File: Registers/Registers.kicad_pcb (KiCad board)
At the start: 2 copper layers, 89.5 x 49.2 mm, 31 parts, among them J1 Conn_01x08_Socket, J2 Conn_01x08_Socket, J3 Conn_01x06_Pin, U1 SN74HCT245N, U2 74LS173, U3 74LS173

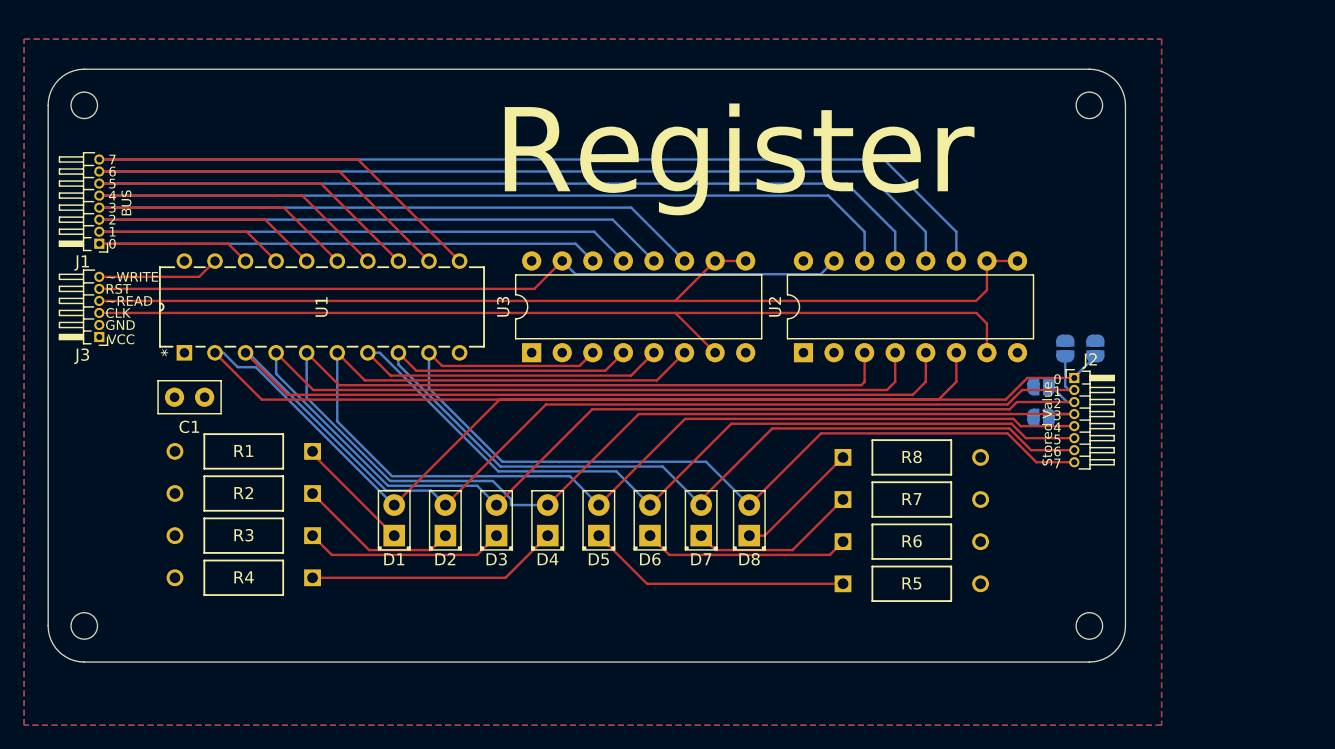
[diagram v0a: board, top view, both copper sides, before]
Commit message: Finished routing for registers. Silkscreen and PCB shape needs to be finalized.
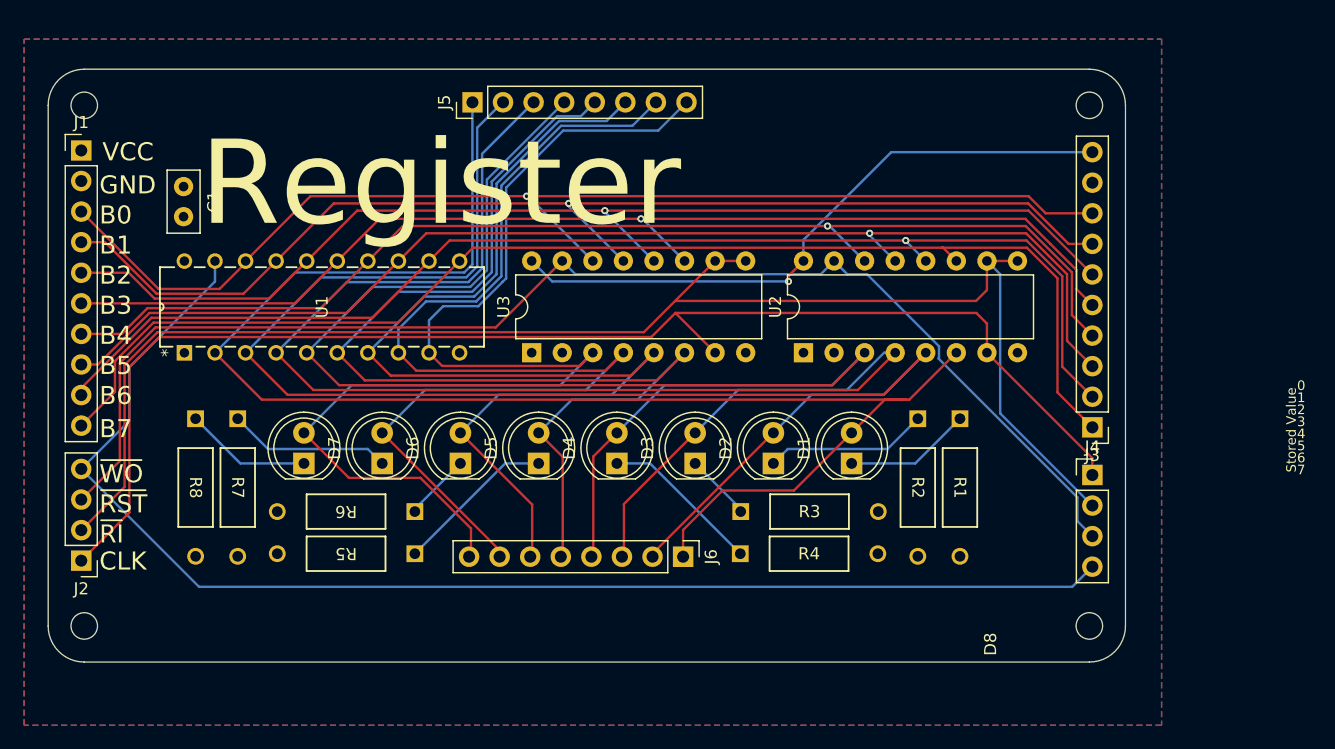
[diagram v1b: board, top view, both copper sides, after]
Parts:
- removed JP1, JP2, JP3, JP4: SolderJumper_2_Open, Jumper:SolderJumper-2_P1.3mm_Open_RoundedPad1.0x1.5mm
- added J4: Conn_01x04_Pin, Connector_PinHeader_2.54mm:PinHeader_1x04_P2.54mm_Vertical, F.Cu at (149.0, 74.0)
- added J5: Conn_01x08_Pin, Connector_PinHeader_2.54mm:PinHeader_1x08_P2.54mm_Vertical, F.Cu at (97.5, 43.0)
- added J6: Conn_01x08_Pin, Connector_PinHeader_2.54mm:PinHeader_1x08_P2.54mm_Vertical, F.Cu at (115.0, 80.8)
- D1, D2, D3, D4, D5, D6, D7, D8: footprint LED_THT:LED_D2.0mm_W4.8mm_H2.5mm_FlatTop -> LED_THT:LED_D5.0mm
- J1: value Conn_01x08_Socket -> Conn_01x10_Pin; footprint Connector_PinHeader_1.00mm:PinHeader_1x08_P1.00mm_Horizontal -> Connector_PinHeader_2.54mm:PinHeader_1x10_P2.54mm_Vertical
- J2: value Conn_01x08_Socket -> Conn_01x04_Pin; footprint Connector_PinHeader_1.00mm:PinHeader_1x08_P1.00mm_Horizontal -> Connector_PinHeader_2.54mm:PinHeader_1x04_P2.54mm_Vertical
- J3: value Conn_01x06_Pin -> Conn_01x10_Pin; footprint Connector_PinHeader_1.00mm:PinHeader_1x06_P1.00mm_Horizontal -> Connector_PinHeader_2.54mm:PinHeader_1x10_P2.54mm_Vertical
- moved J2 83.9 mm to (65.0, 81.1), turned to 180 degrees
- moved J3 82.8 mm to (149.0, 70.0)
- moved R8 53.9 mm to (74.5, 69.3), turned to -90 degrees
- moved R1 53.9 mm to (138.0, 69.3), turned to -90 degrees
- moved R7 50.7 mm to (78.0, 69.3), turned to -90 degrees
- moved R2 50.7 mm to (134.5, 69.3), turned to -90 degrees
- moved D1 38.5 mm to (129.0, 73.0)
- moved D8 37.5 mm to (83.5, 73.0)
- moved R5 35.7 mm to (92.7, 80.5), turned to 180 degrees
- moved R6 35.7 mm to (92.7, 77.0), turned to 180 degrees
- moved R3 35.6 mm to (119.8, 77.0), turned to 0 degrees
- moved R4 35.6 mm to (119.8, 80.5), turned to 0 degrees
- moved D2 27.9 mm to (122.5, 73.0)
- moved D7 27.2 mm to (90.0, 73.0)
- moved C1 17.6 mm to (73.5, 50.0), turned to -90 degrees
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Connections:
- J1 pad 1: /Bus0 -> +5V
- J1 pad 2: /Bus1 -> GND
- J1 pad 3: /Bus2 -> /Bus0
- J1 pad 4: /Bus3 -> /Bus1
- J1 pad 5: /Bus4 -> /Bus2
- J1 pad 6: /Bus5 -> /Bus3
- J1 pad 7: /Bus6 -> /Bus4
- J1 pad 8: /Bus7 -> /Bus5
- J2 pad 1: Net-(D1-A) -> /CLK
- J2 pad 2: Net-(D2-A) -> /~{READ}
- J2 pad 3: Net-(D3-A) -> /RST
- J2 pad 4: Net-(D4-A) -> /~{WRITE}
- J3 pad 1: +5V -> /Bus7
- J3 pad 2: GND -> /Bus6
- J3 pad 3: /CLK -> /Bus5
- J3 pad 4: /~{READ} -> /Bus4
- J3 pad 5: /RST -> /Bus3
- J3 pad 6: /~{WRITE} -> /Bus2
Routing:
- net /~{WRITE}: track 10.2 -> 110.6 mm
- net +5V: track 0.00 -> 53.0 mm, vias 0 -> 1
- net /RST: track 62.9 -> 109.2 mm
- net /Bus0: track 54.3 -> 98.6 mm, vias 0 -> 1
- net /~{READ}: track 86.3 -> 125.6 mm
- net /Bus1: track 60.2 -> 96.9 mm, vias 0 -> 1
- net /CLK: track 81.2 -> 112.1 mm
- net /Bus2: track 66.2 -> 96.0 mm, vias 0 -> 1
- net /Bus3: track 72.1 -> 96.3 mm, vias 0 -> 1
- net Net-(D1-A): track 149.8 -> 127.9 mm
- net Net-(D8-A): track 78.6 -> 96.9 mm
- net Net-(D2-A): track 142.2 -> 126.0 mm
- net Net-(D5-A): track 103.8 -> 91.2 mm
- net Net-(D3-A): track 134.2 -> 121.8 mm
- net Net-(D6-K): track 17.2 -> 5.57 mm
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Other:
- board text added: "B0"
- board text added: "B1"
- board text added: "B2"
- board text added: "B3"
- board text added: "B4"
- board text added: "B5"
- board text added: "B6"
- board text added: "B7"
- board text added: "~{RI}"
- board text added: "~{RST}"
- board text added: "~{WO}"
- board text removed: "BUS"
- board text removed: "NOTE: I don't think I ordered the D-registers. I think I got ALUs by acciedent instead."
- board text removed: "RST"
- board text removed: "TODO: Update for instruction register"
- board text removed: "~READ"
- board text removed: "~WRITE"

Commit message: Register layout complete.
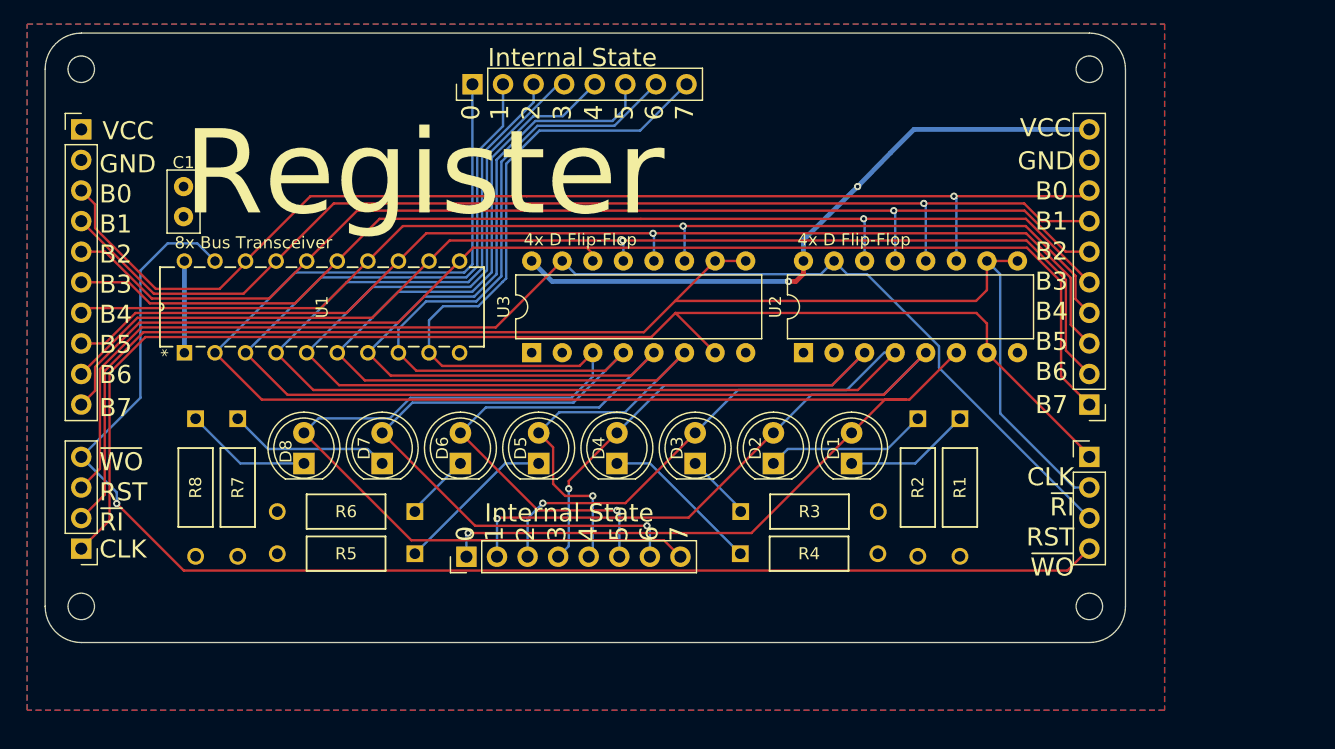
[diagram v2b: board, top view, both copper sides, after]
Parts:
- moved J6 18.0 mm to (97.0, 80.8), turned to 90 degrees
- moved REF** 3.01 mm to (65.0, 40.2)
- moved REF** 3.00 mm to (148.8, 40.2)
- moved C1 2.50 mm to (73.5, 52.5), turned to 90 degrees
- moved J3 1.91 mm to (148.8, 68.1)
- moved J1 1.75 mm to (65.0, 45.2)
- moved REF** 1.64 mm to (65.0, 84.9)
- moved REF** 1.62 mm to (148.8, 84.9)
- moved J4 1.52 mm to (148.8, 72.5)
- moved J5 1.50 mm to (97.5, 41.5)
- moved J2 1.00 mm to (65.0, 80.1)
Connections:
- U2 pad 11: /Bus7 -> /Bus0
- U2 pad 12: /Bus6 -> /Bus1
- U2 pad 13: /Bus5 -> /Bus2
- U2 pad 14: /Bus4 -> /Bus3
- U3 pad 11: /Bus3 -> /Bus4
- U3 pad 12: /Bus2 -> /Bus5
- U3 pad 13: /Bus1 -> /Bus6
- U3 pad 14: /Bus0 -> /Bus7
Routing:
- net Net-(D1-A): track 127.9 -> 147.2 mm, vias 0 -> 1
- net Net-(D8-A): track 96.9 -> 115.8 mm
- net Net-(D2-A): track 126.0 -> 142.1 mm, vias 0 -> 1
- net Net-(D7-A): track 92.8 -> 108.0 mm, vias 0 -> 1
- net Net-(D6-A): track 91.4 -> 101.1 mm, vias 0 -> 1
- net Net-(D3-A): track 121.8 -> 130.5 mm, vias 0 -> 1
- net +5V: track 53.0 -> 61.6 mm, vias 1 -> 2
- net Net-(D5-A): track 91.2 -> 95.5 mm, vias 0 -> 1
- net /Bus4: track 97.8 -> 93.8 mm
- net /Bus6: track 101.8 -> 98.1 mm
- net /~{WRITE}: track 110.6 -> 114.2 mm, vias 0 -> 1
- net /Bus5: track 99.5 -> 95.9 mm
- net /Bus7: track 105.0 -> 101.6 mm
- net /Bus3: track 96.3 -> 93.1 mm
- net Net-(D4-A): track 117.5 -> 120.4 mm, vias 0 -> 1
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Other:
- board size 89.5 x 49.2 mm -> 89.8 x 50.6 mm
- board text added: "4x D Flip-Flop"
- board text added: "8x Bus Transceiver"
- board text added: "Internal State"
- board text added: "RST"
- board text removed: "Stored Value"
- board text removed: "~{RST}"
